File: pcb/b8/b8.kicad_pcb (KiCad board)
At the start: 2 copper layers, 84.6 x 36.3 mm, 30 parts, among them J1 USB, J2 ISP Programming, SW1 SW_Push, SW2 SW_Push, SW3 SW_Push, SW4 SW_Push, SW5 SW_Push, SW6 SW_Push, SW7 SW_Push, SW8 SW_Push, U1 ATtiny4313-P, Y1 20MHz

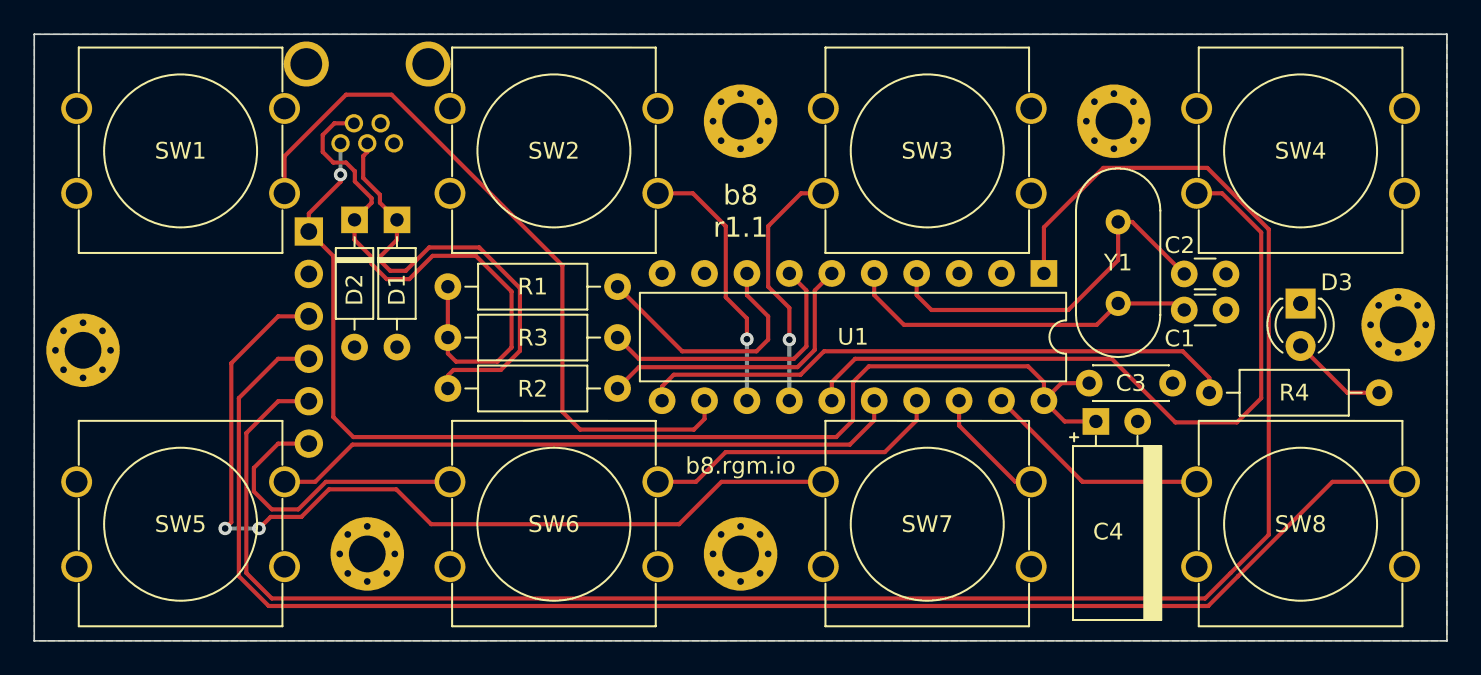
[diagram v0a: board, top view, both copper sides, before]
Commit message: pcb: b8: revision 20240403
some minor pcb fixes. this also moves the pcb files to pcb/b8, preparing
to introduce other pcb variants. this also moves the kicad library to
pcb/lib and adds the missing LICENSE file.
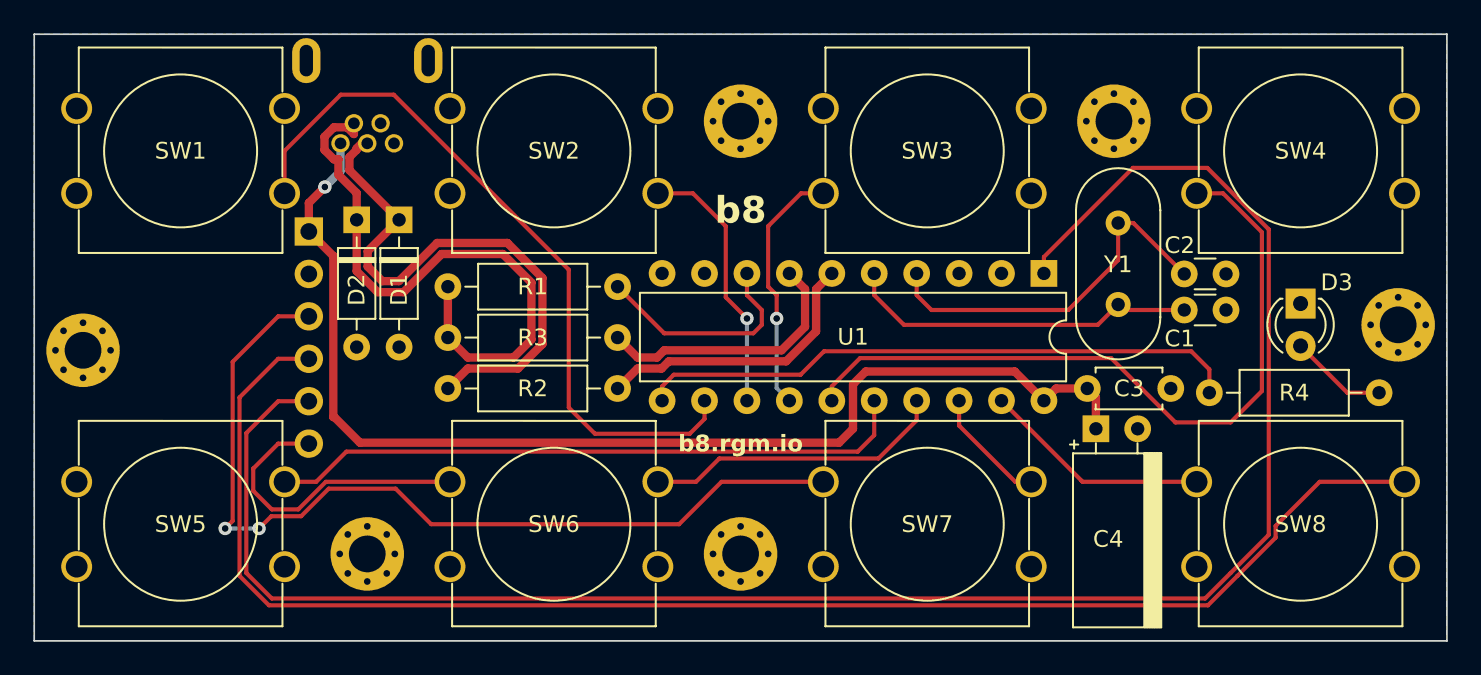
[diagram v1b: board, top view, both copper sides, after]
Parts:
- C3: footprint Capacitor_THT:C_Disc_D4.3mm_W1.9mm_P5.00mm -> b8:C_TDK_FA28
- C4: footprint custom:CP_Radial_D5.0mm_P2.50mm_Horizontal -> b8:CP_Radial_D5.0mm_P2.50mm_Horizontal
- J1: footprint custom:RND_205-00862 -> b8:USB_Mini-B_PTH
- R1, R2, R3, R4: footprint Resistor_THT:R_Axial_DIN0207_L6.3mm_D2.5mm_P10.16mm_Horizontal -> b8:R_YAGEO_MFR-25FTE52_Horizontal
- SW1, SW2, SW3, SW4, SW5, SW6, SW7, SW8: footprint custom:SW_PUSH-12mm -> b8:SW_PUSH-12mm
- Y1: footprint Crystal:Crystal_HC49-U_Vertical -> Crystal:Crystal_HC49-4H_Vertical
- moved C4 0.44 mm to (171.0, 87.0)
- moved C3 0.34 mm to (175.5, 84.6)
- moved D1 0.13 mm to (129.3, 74.5)
- moved D2 0.13 mm to (126.7, 74.5)
- moved Y1 0.06 mm to (172.3, 74.7)
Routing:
- net /USB_CONN_D+: track 28.1 -> 33.4 mm
- net /USB_CONN_D-: track 34.3 -> 36.9 mm
- net USB_PULLUP: track 15.4 -> 13.4 mm
- net +5V: track 72.2 -> 70.5 mm
- net RESET: track 113.6 -> 112.6 mm
- net USB_D-: track 16.9 -> 16.1 mm
- net USB_D+: track 17.8 -> 17.2 mm
- net Net-(U1-PB4): track 38.0 -> 38.5 mm
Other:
- board text added: "Rev: ${REVISION}"
- board text added: "b8"
- board text removed: "b8 r1.1"
